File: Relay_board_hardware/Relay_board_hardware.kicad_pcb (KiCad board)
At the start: 2 copper layers, 90 x 75 mm, 6 parts, among them U1 FTR-F1A, U2 FTR-F1A

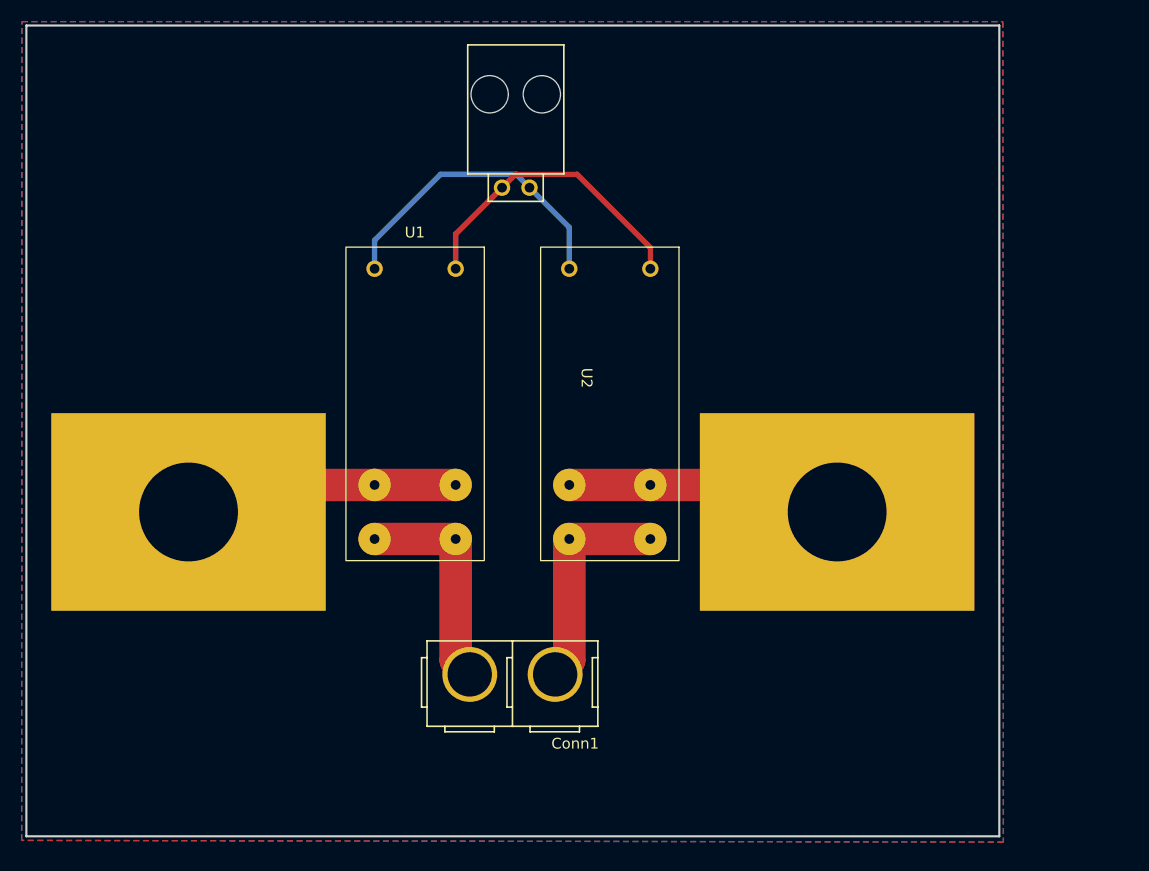
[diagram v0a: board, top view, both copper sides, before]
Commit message: Cleared design
Cleared out the layout for max to take over the design
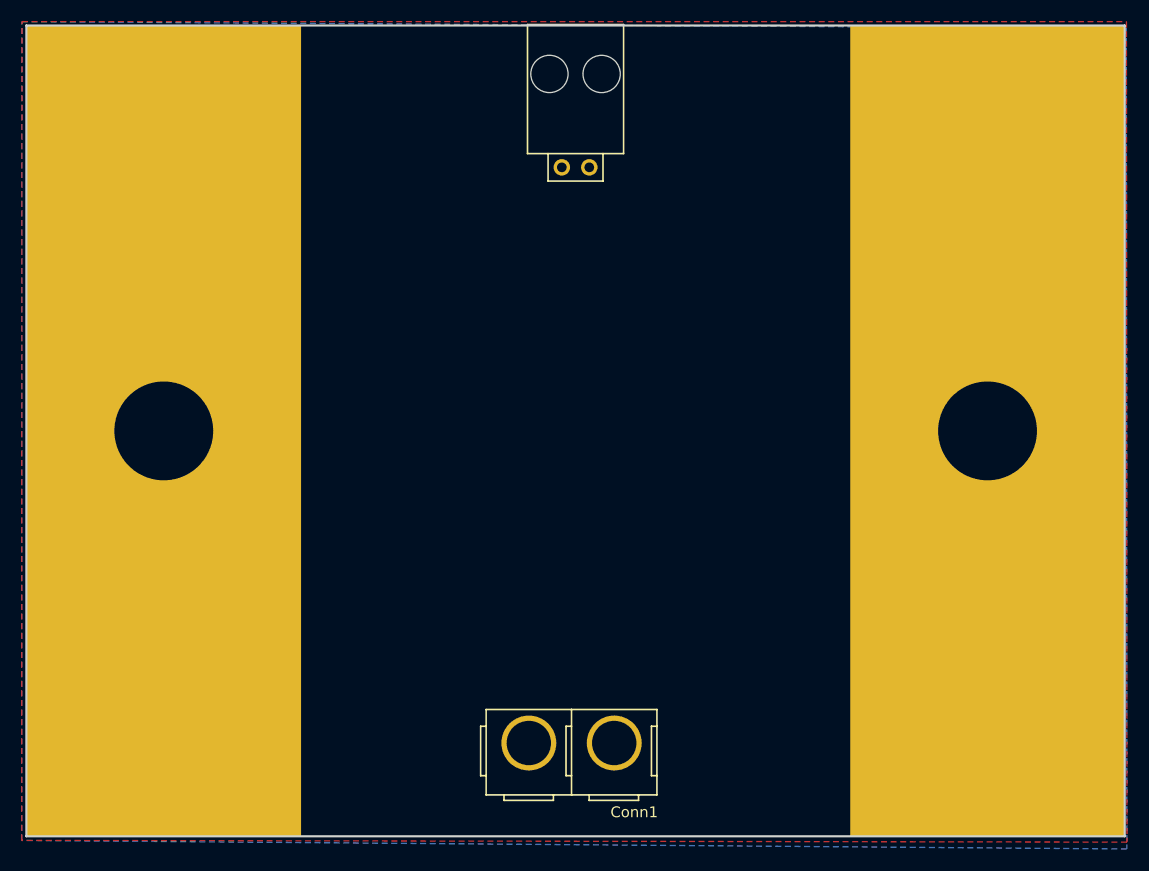
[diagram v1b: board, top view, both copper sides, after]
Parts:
- removed U1, U2: FTR-F1A, Customs:FTR-F1A
- moved V2 15.5 mm to (168.7, 90.2)
- moved Conn1 8.37 mm to (126.5, 116.3)
- moved V1 7.11 mm to (93.2, 90.3)
- moved Conn2 5.84 mm to (129.5, 63.1)
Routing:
- net GND: track 29.0 -> 0.00 mm
- net Net-(U1-Pad5): track 28.3 -> 0.00 mm
- net Net-(U2-Pad2): track 25.8 -> 0.00 mm
- net Net-(U1-Pad2): track 25.7 -> 0.00 mm
- net Net-(Conn1-Pad2): track 20.6 -> 0.00 mm
- net Net-(Conn1-Pad1): track 20.6 -> 0.00 mm
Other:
- board size 90 x 75 mm -> 101.6 x 75 mm

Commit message: board R1
potential changes: anderson placement, IO location, warning correction
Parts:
- added C1: 4.7u, Capacitor_THT:C_Rect_L18.0mm_W9.0mm_P15.00mm_FKS3_FKP3, F.Cu at (129.8, 95.2)
- added Conn3: Molex_SL_02, 0-customs:MOLEX_SL_02_Horizontal, F.Cu at (139.1, 140.1)
- added Conn4: Molex_SL_03, MRDT_Connectors:MOLEX_SL_03_Horizontal, F.Cu at (169.5, 140.1)
- added DANGER!: Symbol_Danger_CopperTop_Small, Symbol:Symbol_Danger_CopperTop_Small, F.Cu at (172.1, 52.1)
- added IC1: BTS3800SL, 0-customs:BTS3800SL, F.Cu at (159.4, 129.2)
- added K1: ~, 0-customs:AECN11012, F.Cu at (149.0, 71.4)
- added K2: ~, 0-customs:AECN11012, F.Cu at (155.8, 134.3)
- added Q1: Q_NMOS_GDS, Package_TO_SOT_SMD:TO-263-2, B.Cu at (137.2, 77.5)
- added R1: R, Resistor_SMD:R_2512_6332Metric_Pad1.40x3.35mm_HandSolder, F.Cu at (171.3, 122.6)
- added R2: R, Resistor_SMD:R_2512_6332Metric_Pad1.40x3.35mm_HandSolder, F.Cu at (162.7, 122.6)
- added REF**: Symbol_HighVoltage_Type2_CopperTop_VerySmall, Symbol:Symbol_HighVoltage_Type2_CopperTop_VerySmall, F.Cu at (170.2, 31.8)
- added REF**: Symbol_HighVoltage_Type2_CopperTop_VerySmall, Symbol:Symbol_HighVoltage_Type2_CopperTop_VerySmall, F.Cu at (168.7, 109.7)
- added REF**: Symbol_HighVoltage_Type2_CopperTop_VerySmall, Symbol:Symbol_HighVoltage_Type2_CopperTop_VerySmall, F.Cu at (134.6, 31.8)
- added REF**: roberto, 0-customs:roberto, F.Cu at (156.7, 139.7)
- added REF**: Symbol_HighVoltage_Type2_CopperTop_Big, Symbol:Symbol_HighVoltage_Type2_CopperTop_Big, F.Cu at (304.8, 72.4)
- added REF**: Symbol_HighVoltage_Type2_CopperTop_VerySmall, Symbol:Symbol_HighVoltage_Type2_CopperTop_VerySmall, B.Cu at (170.2, 31.8)
- added REF**: Symbol_HighVoltage_Type2_CopperTop_VerySmall, Symbol:Symbol_HighVoltage_Type2_CopperTop_VerySmall, B.Cu at (168.7, 109.7)
- added REF**: Symbol_HighVoltage_Type2_CopperTop_VerySmall, Symbol:Symbol_HighVoltage_Type2_CopperTop_VerySmall, B.Cu at (134.6, 31.8)
- added U1: Opamp_Dual, Package_SO:SOIC-8_3.9x4.9mm_P1.27mm, F.Cu at (167.6, 132.4)
- added V3: BATT_PWR_VIA, 0-customs:via, F.Cu at (114.3, 57.1)
- added V4: BATT_PWR_VIA, 0-customs:via, F.Cu at (190.5, 120.7)
- added V5: BATT_PWR_VIA, 0-customs:via, F.Cu at (114.3, 120.7)
- Conn1: footprint Customs:Anderson_2_Vertical_Sidy_by_Side -> 0-customs:Square_Anderson_2_V_Side_By_Side; moved to B.Cu
- Conn2: footprint Customs:MOLEX_SL_02_Horizontal -> 0-customs:MOLEX_SL_02_Horizontal
- V1, V2: value Via -> BATT_PWR_VIA; footprint Customs:via -> 0-customs:via
- moved Conn2 79.4 mm to (149.1, 140.1), turned to 180 degrees
- moved V1 70.5 mm to (152.4, 52.1)
- moved V2 39.6 mm to (190.5, 57.1)
- moved Conn1 28.7 mm to (152.4, 104.0), turned to 180 degrees
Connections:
- Conn1 pad 1: Net-(Conn1-Pad1) -> /RLY_V+
- Conn1 pad 2: Net-(Conn1-Pad2) -> /RLY_V-
- Conn2 pad 1: Net-(U1-Pad5) -> /RLY_IN
- V1 pad 1: Net-(U1-Pad2) -> /PWRRES
- V2 pad 1: Net-(U2-Pad2) -> VBUS
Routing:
- net GND: track 0.00 -> 79.9 mm, vias 0 -> 7
- net /DSCHG_IN: track 0.00 -> 61.8 mm
- net GNDPWR: track 0.00 -> 25.9 mm
- net /RLY_V+: track 0.00 -> 18.7 mm
- net /RLY_V-: track 0.00 -> 17.4 mm
- net VBUS: track 0.00 -> 16.9 mm
- net Net-(U1A--): track 0.00 -> 15.8 mm, vias 0 -> 1
- net /RLY_IN: track 0.00 -> 13.7 mm
- net Net-(U1A-+): track 0.00 -> 9.91 mm
- net Net-(IC1-DRAIN): track 0.00 -> 5.81 mm
- net /PWRRES: vias 0 -> 9
- added copper zone on B.Cu, net /PWRRES
- added copper zone on F.Cu, net /PWRRES
- added copper zone on B.Cu, net GNDPWR
- added copper zone on F.Cu, net GNDPWR
- added copper zone on B.Cu, net VBUS
- added copper zone on F.Cu, net VBUS
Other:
- board size 101.6 x 75 mm -> 101.6 x 127 mm
- board text added: "GND S/VCC"
- board text added: "GND/S"
- board text added: "Relay and Interfaces Board, R1 {dblquote}Kintetic Antenna{dblquote} Senior Design 23-24 Missouri S&T ECE Department"
- board text added: "S/GND"
- board text added: "V+"
- board text added: "V-"

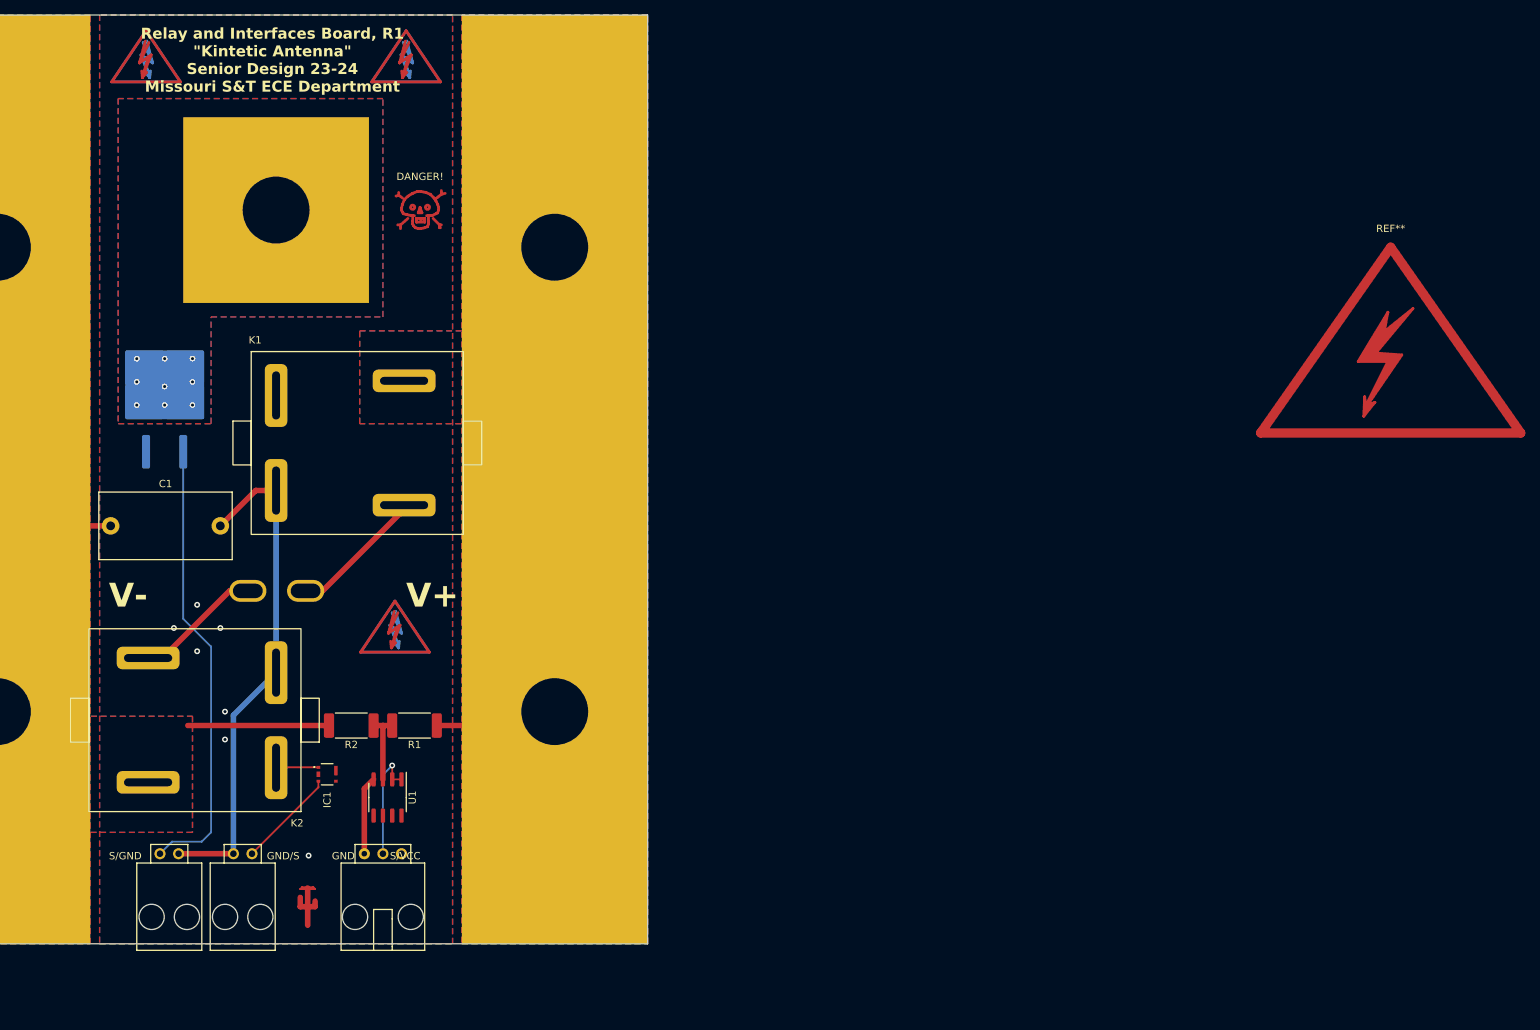
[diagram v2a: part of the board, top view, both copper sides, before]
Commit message: side-by-side-R1
complete board design with the relays situated side-by-side
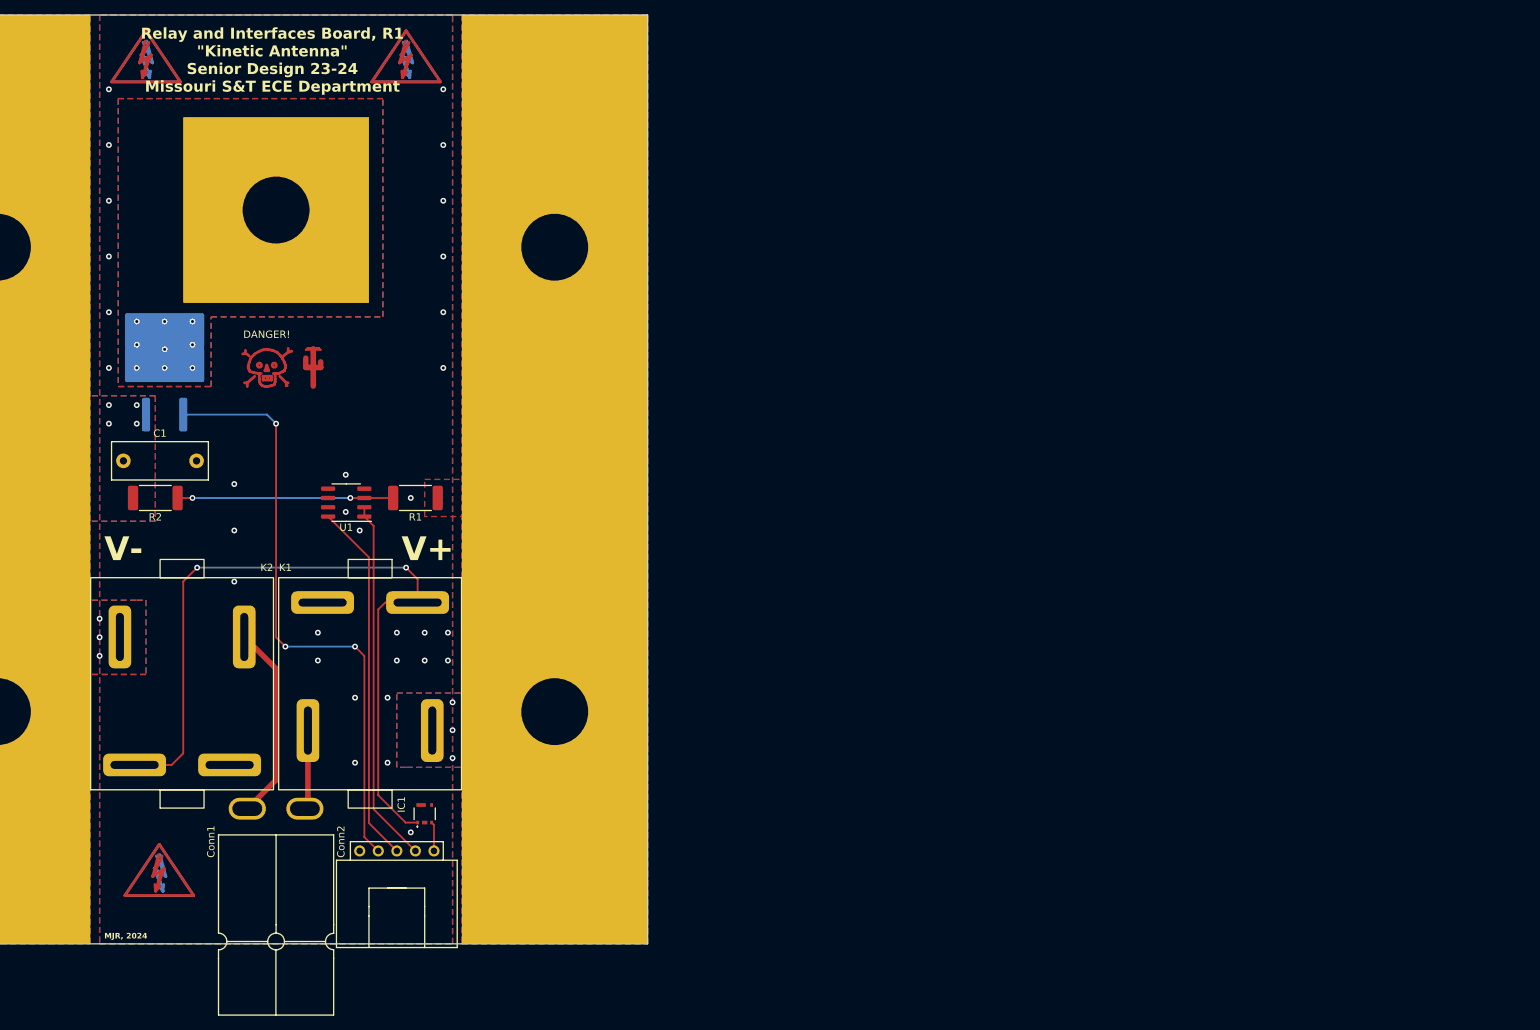
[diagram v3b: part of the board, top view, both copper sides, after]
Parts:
- removed Conn3: Molex_SL_02, 0-customs:MOLEX_SL_02_Horizontal
- removed Conn4: Molex_SL_03, MRDT_Connectors:MOLEX_SL_03_Horizontal
- removed the REF** at (304.8, 72.4)
- C1: footprint Capacitor_THT:C_Rect_L18.0mm_W9.0mm_P15.00mm_FKS3_FKP3 -> Capacitor_THT:C_Rect_L13.0mm_W5.0mm_P10.00mm_FKS3_FKP3_MKS4
- Conn1: value Anderson -> AndersonPP; footprint 0-customs:Square_Anderson_2_V_Side_By_Side -> 0-customs:Square_Anderson_2_H_Side_By_Side; moved to F.Cu
- Conn2: value Molex_SL_02 -> Molex_SL_05; footprint 0-customs:MOLEX_SL_02_Horizontal -> 0-customs:MOLEX_SL_05_Horizontal
- V1: footprint 0-customs:via -> 0-customs:via_L1000mil_W1000mil
- V2, V3, V4, V5: footprint 0-customs:via -> 0-customs:via_L2500mil_W1000mil
- moved REF** 73.7 mm to (157.5, 66.0)
- moved REF** 46.3 mm to (136.4, 143.0) (x2)
- moved K1 42.2 mm to (177.8, 102.3), turned to -90 degrees
- moved R2 41.1 mm to (135.9, 91.4)
- moved U1 40.7 mm to (162.0, 92.1), turned to 180 degrees
- moved R1 31.1 mm to (171.4, 91.4)
- moved DANGER! 30.1 mm to (151.1, 73.7)
- moved Conn1 29.9 mm to (147.9, 133.5), turned to 90 degrees
- moved K2 28.9 mm to (127.0, 131.3), turned to 90 degrees
- moved Conn2 24.9 mm to (174.0, 139.7)
- moved IC1 14.4 mm to (172.7, 134.6), turned to 0 degrees
- moved C1 9.06 mm to (131.5, 86.4)
- moved Q1 5.08 mm to (137.2, 72.4)
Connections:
- net /RLY_IN renamed RLY_IN
- Conn1 pad 1: /RLY_V+ -> /RLY_V-
- Conn1 pad 2: /RLY_V- -> /RLY_V+
- Conn2 pad 2: GND -> /V_SENSE_OUT
- Q1 pad 1: /DSCHG_IN -> DSCHG_IN
- U1 pad 1: Net-(U1A--) -> /V_SENSE_OUT
- U1 pad 2: Net-(U1A--) -> /V_SENSE_OUT
- U1 pad 8: +5V -> +3V3
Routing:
- net Net-(IC1-DRAIN): track 5.81 -> 105.6 mm, vias 0 -> 2
- net DSCHG_IN: track 0.00 -> 83.0 mm, vias 0 -> 3
- net GND: track 79.9 -> 0.00 mm, vias 7 -> 32
- net /DSCHG_IN: track 61.8 -> 0.00 mm
- net /V_SENSE_OUT: track 0.00 -> 49.9 mm
- net +3V3: track 0.00 -> 49.6 mm
- net GNDPWR: track 25.9 -> 0.00 mm, vias 0 -> 7
- net Net-(U1A-+): track 9.91 -> 29.5 mm, vias 0 -> 2
- net VBUS: track 16.9 -> 0.00 mm, vias 0 -> 3
- net Net-(U1A--): track 15.8 -> 0.00 mm, vias 1 -> 0
- net RLY_IN: track 13.7 -> 4.01 mm
- net /RLY_V-: track 17.4 -> 26.9 mm
- net /RLY_V+: track 18.7 -> 10.9 mm
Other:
- board text added: "MJR, 2024"
- board text added: "Relay and Interfaces Board, R1 {dblquote}Kinetic Antenna{dblquote} Senior Design 23-24 Missouri S&T ECE Department"
- board text removed: "GND S/VCC"
- board text removed: "GND/S"
- board text removed: "Relay and Interfaces Board, R1 {dblquote}Kintetic Antenna{dblquote} Senior Design 23-24 Missouri S&T ECE Department"
- board text removed: "S/GND"
